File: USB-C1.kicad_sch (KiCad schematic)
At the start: 32 parts, among them J2 USB_C_Receptacle, J3 I2C_HD3SS3220, U3 HD3SS3220IRNHR, U4 TPS2068EDBVR, U5 TPD4E02B04DQA, U6 TPD4E02B04DQA, U7 TPD4E02B04DQA

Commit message: comments to schematic added, changed a few components
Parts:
- J2: Mouser Part No  (none) -> 640-USB4200-03-A
- R11: footprint Resistor_SMD:R_0402_1005Metric -> Resistor_SMD:R_1206_3216Metric; Mouser Part No  (none) -> 603-RT1206CRE07900KL
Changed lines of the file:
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@@
 			)
 		)
-		(property "Footprint" "Resistor_SMD:R_0402_1005Metric"
+		(property "Footprint" "Resistor_SMD:R_1206_3216Metric"
 			(at 50.038 45.72 90)
 			(effects
@@
 		)
 		(property "Description" "Resistor"
+			(at 48.26 45.72 0)
+			(effects
+				(font
+					(size 1.27 1.27)
+				)
+				(hide yes)
+			)
+		)
+		(property "Mouser Part No " "603-RT1206CRE07900KL "
 			(at 48.26 45.72 0)
 			(effects
@@
 			(at 248.92 50.8 0)
 			(effects
+				(font
+					(size 1.27 1.27)
+				)
+				(hide yes)
+			)
+		)
+		(property "Mouser Part No " "640-USB4200-03-A "
+			(at 248.92 50.8 0)
+			(effects

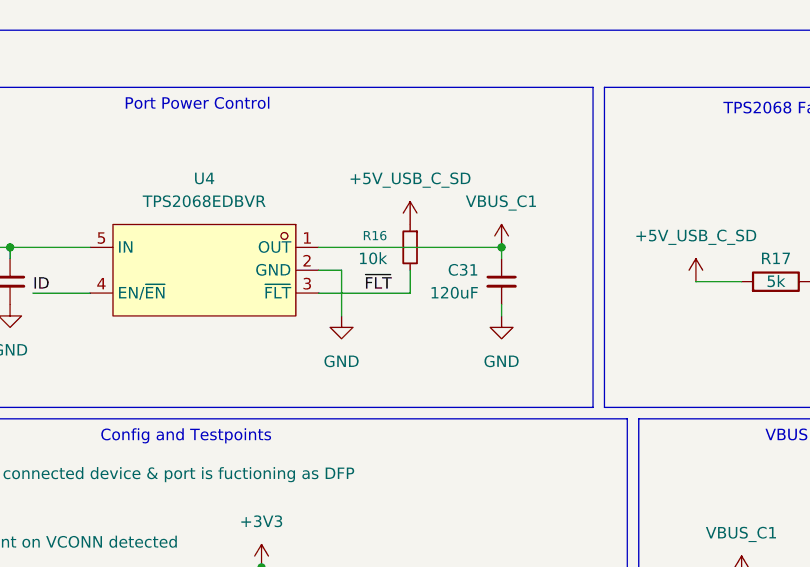
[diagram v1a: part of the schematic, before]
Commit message: AP7361C'sOO footprint changed, Inductors footprint improved
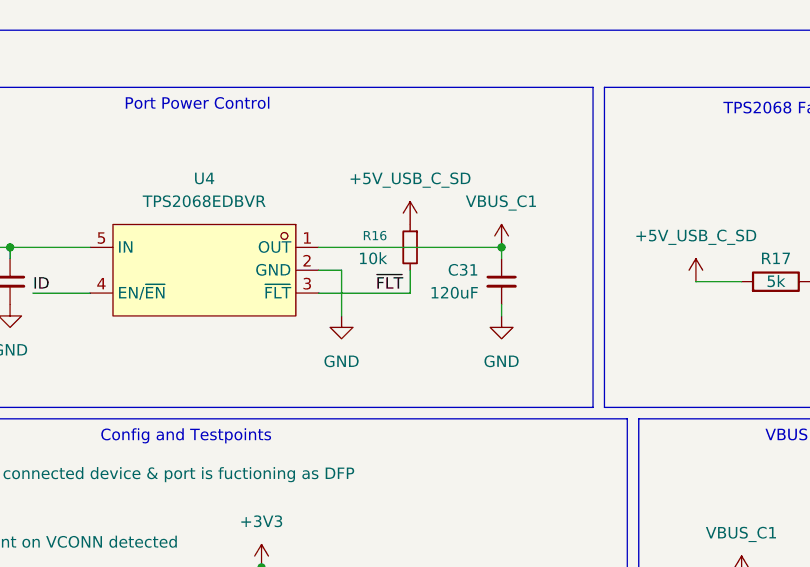
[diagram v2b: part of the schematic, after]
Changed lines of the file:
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@@
 	)
 	(label "~{FLT}"
-		(at 76.2 134.62 0)
+		(at 77.47 134.62 0)
 		(effects
 			(font

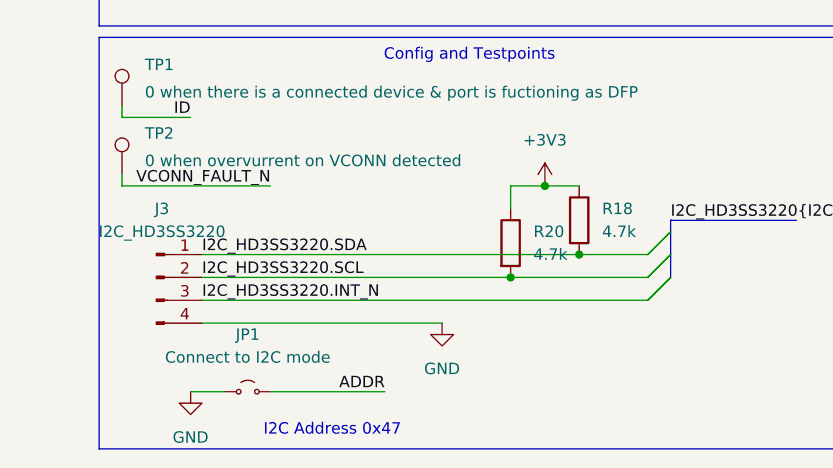
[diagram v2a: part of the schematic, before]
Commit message: Rearrange of the component placement, scheme changes for better routing
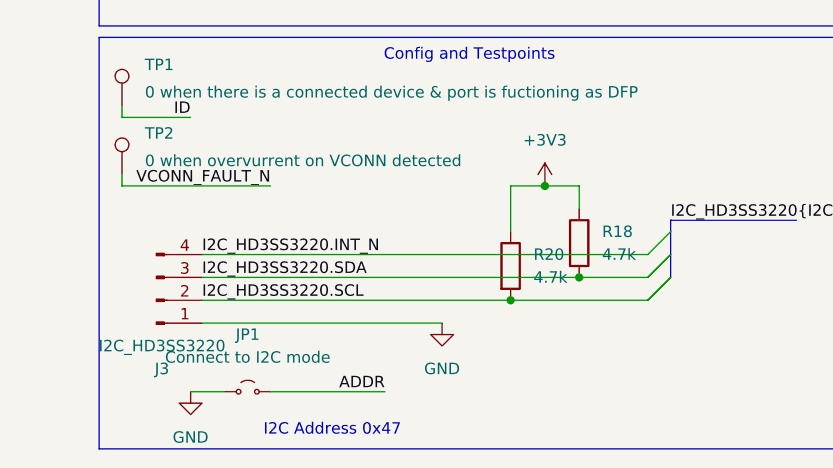
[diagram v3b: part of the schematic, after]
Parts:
- C24, C25, C26, C27, C28, C30: footprint Capacitor_SMD:C_0402_1005Metric -> Capacitor_SMD:C_0201_0603Metric; LCSC Part C5182432 -> C181043
- J3: footprint Connector_PinHeader_1.27mm:PinHeader_1x03_P1.27mm_Vertical -> Connector_PinHeader_1.00mm:PinHeader_1x04_P1.00mm_Vertical
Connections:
- net GND: now also J3.1 (Pin_1); no longer J3.4 (Pin_4)
- net I2C_HD3SS3220.INT_N: now also J3.4 (Pin_4); no longer J3.3 (Pin_3)
- net I2C_HD3SS3220.SDA: now also J3.3 (Pin_3); no longer J3.1 (Pin_1)
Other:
- moved on the sheet: R18, R20
